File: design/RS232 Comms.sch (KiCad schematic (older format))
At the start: 8 parts

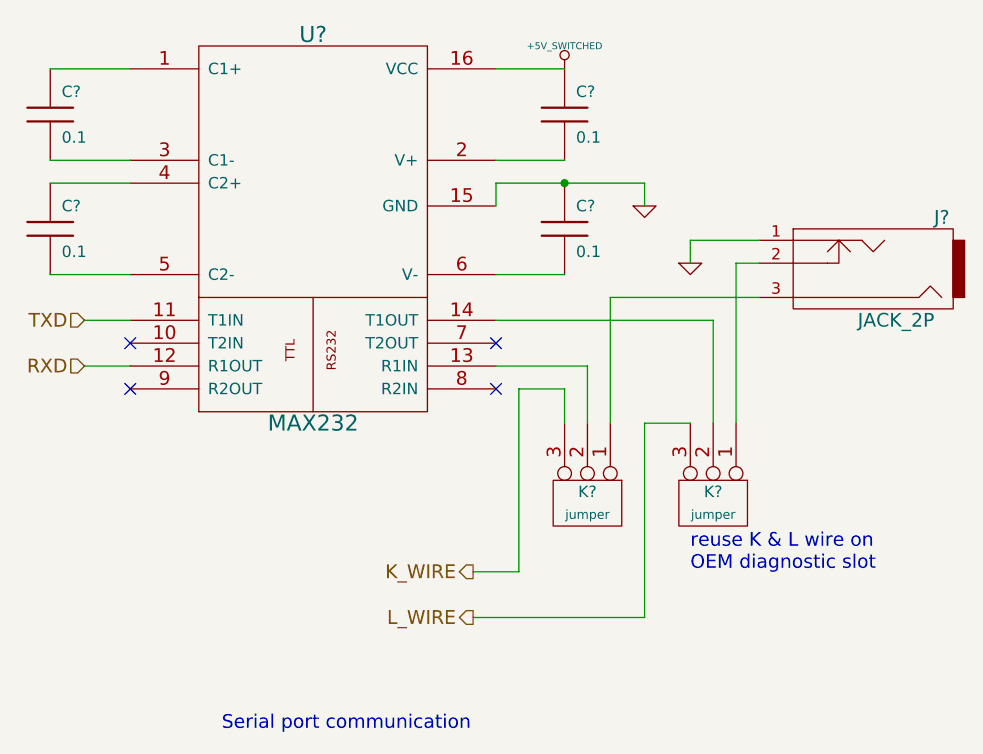
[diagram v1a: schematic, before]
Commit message: revise schema to be full pin compatible with stock ECU
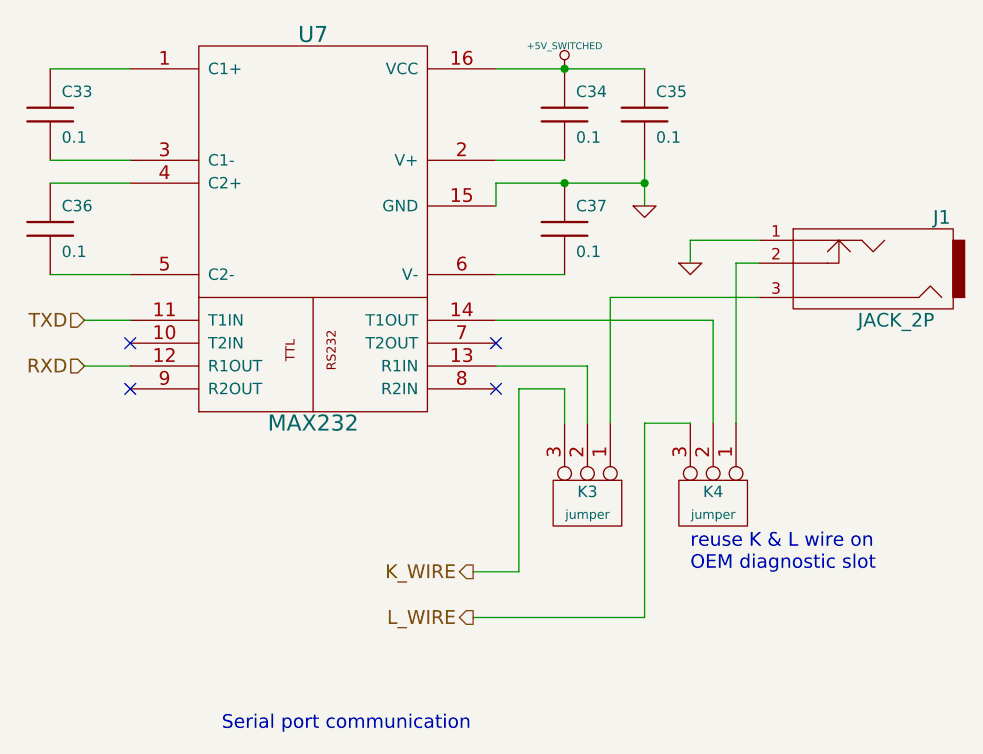
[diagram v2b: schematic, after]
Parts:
- added C35: 0.1, symbol C
- gave numbers to parts that had none: 8
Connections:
- net +5V_SWITCHED: now also C35.1
- net GND: now also C35.2
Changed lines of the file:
@@
-EESchema Schematic File Version 2  date 27/12/2011 00:52:12
+EESchema Schematic File Version 2  date 02/01/2012 14:25:41
 LIBS:power
 LIBS:device
@@
 EELAYER END
 $Descr A4 11700 8267
-Sheet 7 12
+Sheet 8 12
 Title ""
-Date "26 dec 2011"
+Date "2 jan 2012"
 Rev ""
 Comp ""
@@
 Comment4 ""
 $EndDescr
+Connection ~ 6700 3150
+Wire Wire Line
+	6700 3050 6700 3250
+Wire Wire Line
+	6900 3500 6900 3400
+Wire Wire Line
+	6900 3400 7200 3400
+Wire Wire Line
+	7200 3500 7100 3500
+Wire Wire Line
+	7100 3500 7100 4200
+Wire Wire Line
+	6700 4200 6700 5050
+Wire Wire Line
+	6700 4200 6900 4200
+Wire Wire Line
+	6350 4200 6350 4050
+Wire Wire Line
+	6350 4050 6150 4050
+Wire Wire Line
+	6700 3150 6050 3150
+Wire Wire Line
+	4450 3950 4250 3950
+Wire Wire Line
+	6050 3150 6050 3250
+Wire Wire Line
+	4100 3150 4450 3150
+Wire Wire Line
+	4100 3050 4450 3050
+Wire Wire Line
+	4100 2650 4450 2650
+Wire Wire Line
+	4100 3550 4450 3550
+Wire Wire Line
+	6050 3050 6350 3050
+Wire Wire Line
+	6350 3550 6050 3550
+Connection ~ 6350 3150
+Wire Wire Line
+	4450 3750 4250 3750
+Wire Wire Line
+	6050 3950 6450 3950
+Wire Wire Line
+	6450 3950 6450 4200
+Wire Wire Line
+	6700 5050 5950 5050
+Wire Wire Line
+	6150 4050 6150 4850
+Wire Wire Line
+	6150 4850 5950 4850
+Wire Wire Line
+	7000 4200 7000 3750
+Wire Wire Line
+	7000 3750 6050 3750
+Wire Wire Line
+	6550 4200 6550 3650
+Wire Wire Line
+	6550 3650 7200 3650
+Wire Wire Line
+	6700 2650 6050 2650
+Connection ~ 6350 2650
+$Comp
+L C C35
+U 1 1 4F011FB1
+P 6700 2850
+F 0 "C35" H 6750 2950 50  0000 L CNN
+F 1 "0.1" H 6750 2750 50  0000 L CNN
+	1    6700 2850
+	1    0    0    -1
+$EndComp
 Text HLabel 5950 5050 0    60   Output ~ 0
 L_WIRE
 Text HLabel 5950 4850 0    60   Output ~ 0
 K_WIRE
-Wire Wire Line
-	6900 3500 6900 3400
-Wire Wire Line
-	6900 3400 7200 3400
-Wire Wire Line
-	7200 3500 7100 3500
-Wire Wire Line
-	7100 3500 7100 4200
-Wire Wire Line
-	6700 4200 6700 5050
-Wire Wire Line
-	6700 4200 6900 4200
-Wire Wire Line
-	6350 4200 6350 4050
-Wire Wire Line
-	6350 4050 6150 4050
-Wire Wire Line
-	6700 3250 6700 3150
-Wire Wire Line
-	6700 3150 6350 3150
-Wire Wire Line
-	6350 3150 6050 3150
-Wire Wire Line
-	4450 3950 4250 3950
-Wire Wire Line
-	6050 3150 6050 3250
-Wire Wire Line
-	6350 2650 6050 2650
-Wire Wire Line
-	4100 3150 4450 3150
-Wire Wire Line
-	4100 3050 4450 3050
-Wire Wire Line
-	4100 2650 4450 2650
-Wire Wire Line
-	4100 3550 4450 3550
-Wire Wire Line
-	6050 3050 6350 3050
-Wire Wire Line
-	6350 3550 6050 3550
-Connection ~ 6350 3150
-Wire Wire Line
-	4450 3750 4250 3750
-Wire Wire Line
-	6050 3950 6450 3950
-Wire Wire Line
-	6450 3950 6450 4200
-Wire Wire Line
-	6700 5050 5950 5050
-Wire Wire Line
-	6150 4050 6150 4850
-Wire Wire Line
-	6150 4850 5950 4850
-Wire Wire Line
-	7000 4200 7000 3750
-Wire Wire Line
-	7000 3750 6050 3750
-Wire Wire Line
-	6550 4200 6550 3650
-Wire Wire Line
-	6550 3650 7200 3650
-$Comp
-L CONN_3 K?
+$Comp
+L CONN_3 K3
 U 1 1 4E927716
 P 6450 4550
-F 0 "K?" V 6400 4550 50  0000 C CNN
+F 0 "K3" V 6400 4550 50  0000 C CNN
 F 1 "jumper" V 6500 4550 40  0000 C CNN
 	1    6450 4550
@@
 $EndComp
 $Comp
-L CONN_3 K?
+L CONN_3 K4
 U 1 1 4E927715
 P 7000 4550
-F 0 "K?" V 6950 4550 50  0000 C CNN
+F 0 "K4" V 6950 4550 50  0000 C CNN
 F 1 "jumper" V 7050 4550 40  0000 C CNN
 	1    7000 4550
@@
 $EndComp
 $Comp
-L GND #PWR?
+L GND #PWR087
 U 1 1 4E92FFAF
 P 6900 3500
-F 0 "#PWR?" H 6900 3500 30  0001 C CNN
+F 0 "#PWR087" H 6900 3500 30  0001 C CNN
 F 1 "GND" H 6900 3430 30  0001 C CNN
 	1    6900 3500
@@
 $EndComp
 $Comp
-L JACK_2P J?
+L JACK_2P J1
 U 1 1 4E927849
 P 7650 3500
-F 0 "J?" H 7300 3300 60  0000 C CNN
+F 0 "J1" H 7300 3300 60  0000 C CNN
 F 1 "JACK_2P" H 7500 3750 60  0000 C CNN
 	1    7650 3500
@@
 $EndComp
 $Comp
-L +5V_SWITCHED #PWR?
+L +5V_SWITCHED #PWR088
 U 1 1 4E9277BA
 P 6350 2650
-F 0 "#PWR?" H 6350 2600 20  0001 C CNN
+F 0 "#PWR088" H 6350 2600 20  0001 C CNN
 F 1 "+5V_SWITCHED" H 6350 2750 30  0000 C CNN
 	1    6350 2650
@@
 $EndComp
 $Comp
-L MAX232 U?
+L MAX232 U7
 U 1 1 4E92771D
 P 5250 3350
-F 0 "U?" H 5250 4200 70  0000 C CNN
+F 0 "U7" H 5250 4200 70  0000 C CNN
 F 1 "MAX232" H 5250 2500 70  0000 C CNN
 	1    5250 3350
@@
 $EndComp
 $Comp
-L C C?
+L C C36
 U 1 1 4E92771C
 P 4100 3350
-F 0 "C?" H 4150 3450 50  0000 L CNN
+F 0 "C36" H 4150 3450 50  0000 L CNN
 F 1 "0.1" H 4150 3250 50  0000 L CNN
 	1    4100 3350
@@
 $EndComp
 $Comp
-L C C?
+L C C34
 U 1 1 4E92771B
 P 6350 2850
-F 0 "C?" H 6400 2950 50  0000 L CNN
+F 0 "C34" H 6400 2950 50  0000 L CNN
 F 1 "0.1" H 6400 2750 50  0000 L CNN
 	1    6350 2850
@@
 $EndComp
 $Comp
-L C C?
+L C C37
 U 1 1 4E92771A
 P 6350 3350
-F 0 "C?" H 6400 3450 50  0000 L CNN
+F 0 "C37" H 6400 3450 50  0000 L CNN
 F 1 "0.1" H 6400 3250 50  0000 L CNN
 	1    6350 3350
@@
 $EndComp
 $Comp
-L C C?
+L C C33
 U 1 1 4E927719
 P 4100 2850
-F 0 "C?" H 4150 2950 50  0000 L CNN
+F 0 "C33" H 4150 2950 50  0000 L CNN
 F 1 "0.1" H 4150 2750 50  0000 L CNN
 	1    4100 2850
@@
 Serial port communication
 $Comp
-L GND #PWR?
+L GND #PWR089
 U 1 1 4E927717
 P 6700 3250
-F 0 "#PWR?" H 6700 3250 30  0001 C CNN
+F 0 "#PWR089" H 6700 3250 30  0001 C CNN
 F 1 "GND" H 6700 3180 30  0001 C CNN
 	1    6700 3250
